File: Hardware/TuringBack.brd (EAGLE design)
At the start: 107 x 49.5 mm, 45 parts, among them IC11 78L09, IC12 78L09, IC7 TL072P

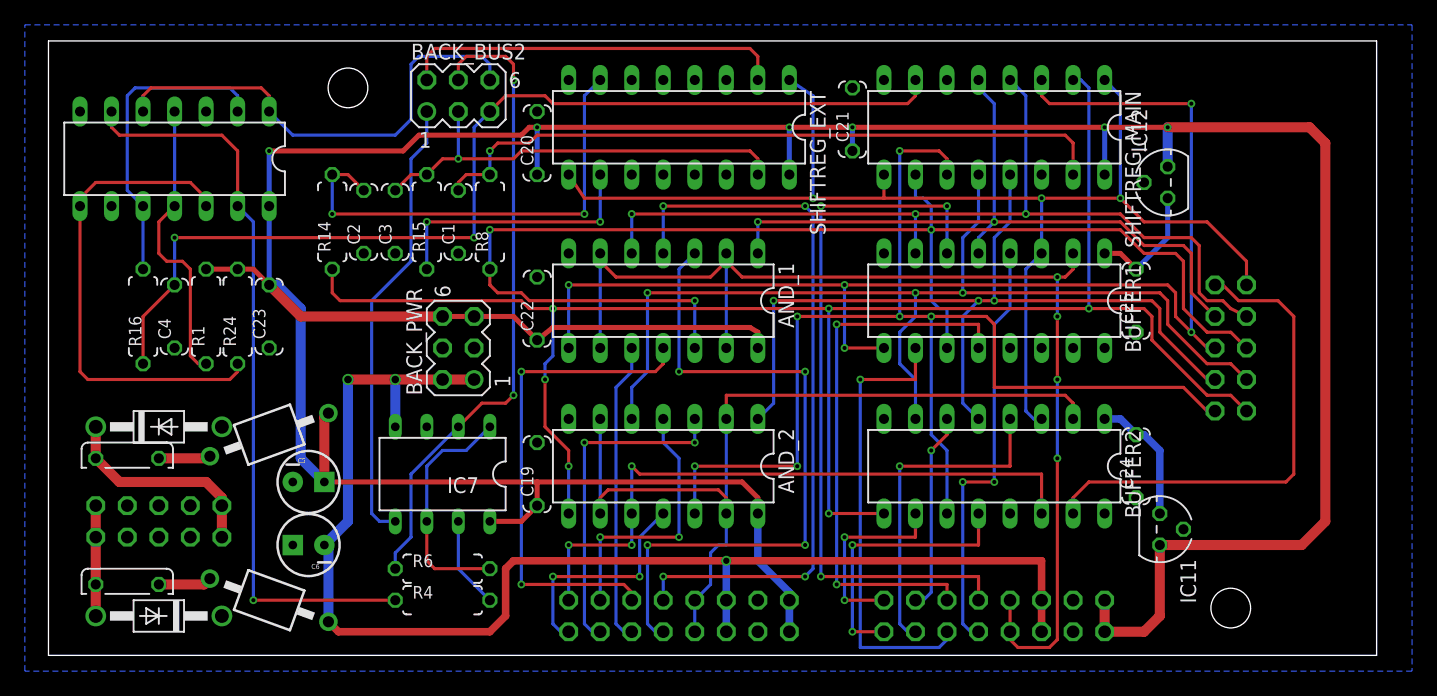
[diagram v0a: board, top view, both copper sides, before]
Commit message: Starting to route front board
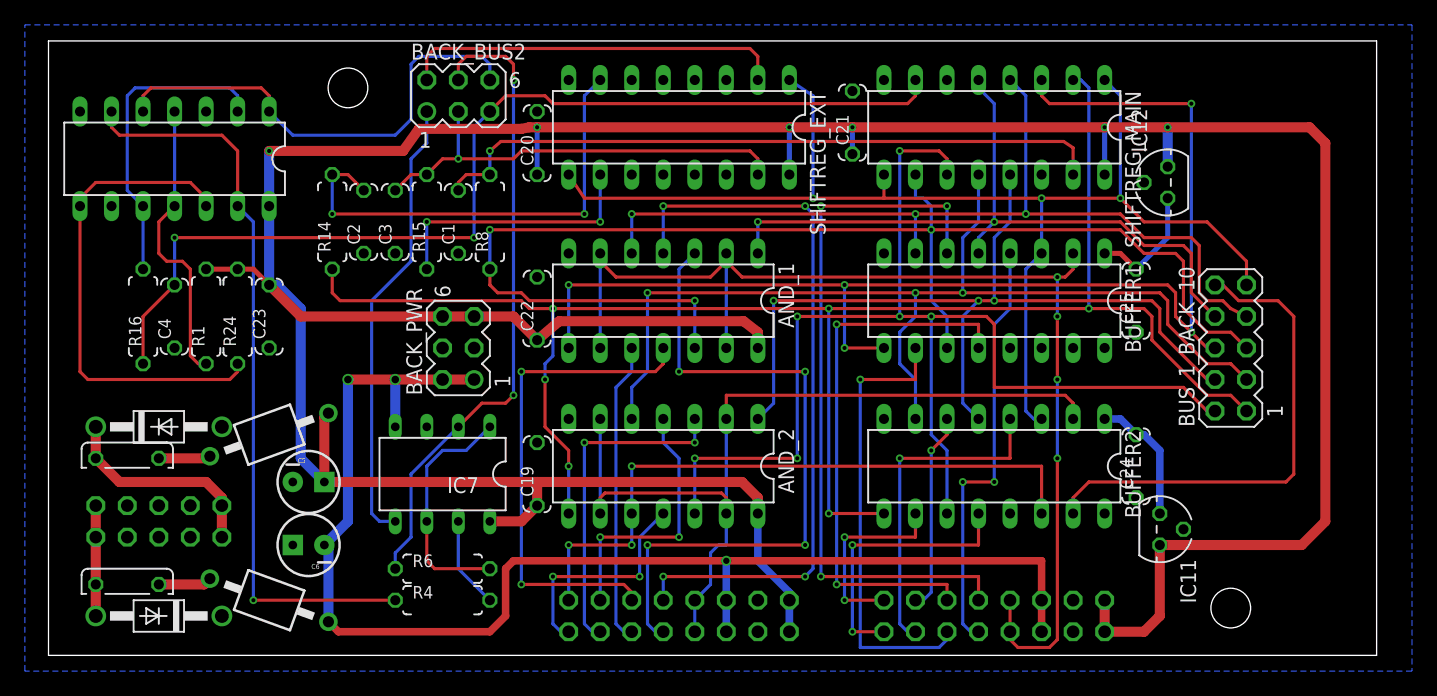
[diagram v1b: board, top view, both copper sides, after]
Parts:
- BUS_1_BACK: device MusicThingModular:10PIN_BACKSIDE -> con-lstb:MA05-2
- moved C21 0.25 mm to (64.8, 42.9)
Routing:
- net +12V_BACK: track 297.4 -> 298.2 mm
- net N$10: track 55.7 -> 54.9 mm
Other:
- board text added: "Music Thing Modular Turing Machine Rev4 Prototype 1 Designed in Herne Hill, London By Tom Whitwell August 2015 CC-BY-SA"

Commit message: routing tweaks on back panel
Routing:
- net BUFFCLK2_BACK: track 94.4 -> 91.2 mm, vias 4 -> 3
- net GATE8: track 34.4 -> 33.0 mm, vias 2 -> 0
- net PULSE7: vias 4 -> 3
- net PULSE4: vias 2 -> 1
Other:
- board text added: "FERRITE BEAD"

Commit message: Routing tweaks
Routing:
- net +12V_BACK: track 298.2 -> 247.9 mm, vias 6 -> 3
- net B1_BACK: track 138.5 -> 167.3 mm, vias 6 -> 2
- net PULSE8: track 54.8 -> 32.8 mm, vias 4 -> 0
- net N$10: track 54.9 -> 71.4 mm, vias 1 -> 0
- net CLOCK_BACK: track 101.3 -> 117.5 mm, vias 3 -> 1
- net PULSE5: track 39.5 -> 31.5 mm
- net N$4: track 23.5 -> 29.7 mm
- net N$28: track 37.9 -> 33.0 mm, vias 2 -> 1
- net B5_BACK: track 107.8 -> 103.4 mm, vias 3 -> 2
- net N$7: track 19.4 -> 23.7 mm
- net GATE1: track 15.9 -> 12.2 mm
- net PULSE_OUT_BACK: track 39.9 -> 36.5 mm
- net PULSE1: track 52.7 -> 49.4 mm, vias 3 -> 2
- net N$2: track 60.4 -> 57.0 mm, vias 1 -> 0
- net -12V_BACK: track 108.2 -> 105.0 mm, vias 3 -> 2
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
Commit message: StillTweaking
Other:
- board text added: "Music Thing Modular Turing Machine Rev4 Prototype 1 Back Board Designed in Herne Hill, London By Tom Whitwell September 2015 CC-BY-SA"
- board text removed: "Music Thing Modular Turing Machine Rev4 Prototype 1 Designed in Herne Hill, London By Tom Whitwell August 2015 CC-BY-SA"
